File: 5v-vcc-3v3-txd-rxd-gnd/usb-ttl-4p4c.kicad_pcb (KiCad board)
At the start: 4 copper layers, 41.3 x 16.5 mm, 3 parts, among them J1 4P4C, P1 CONN_6X1

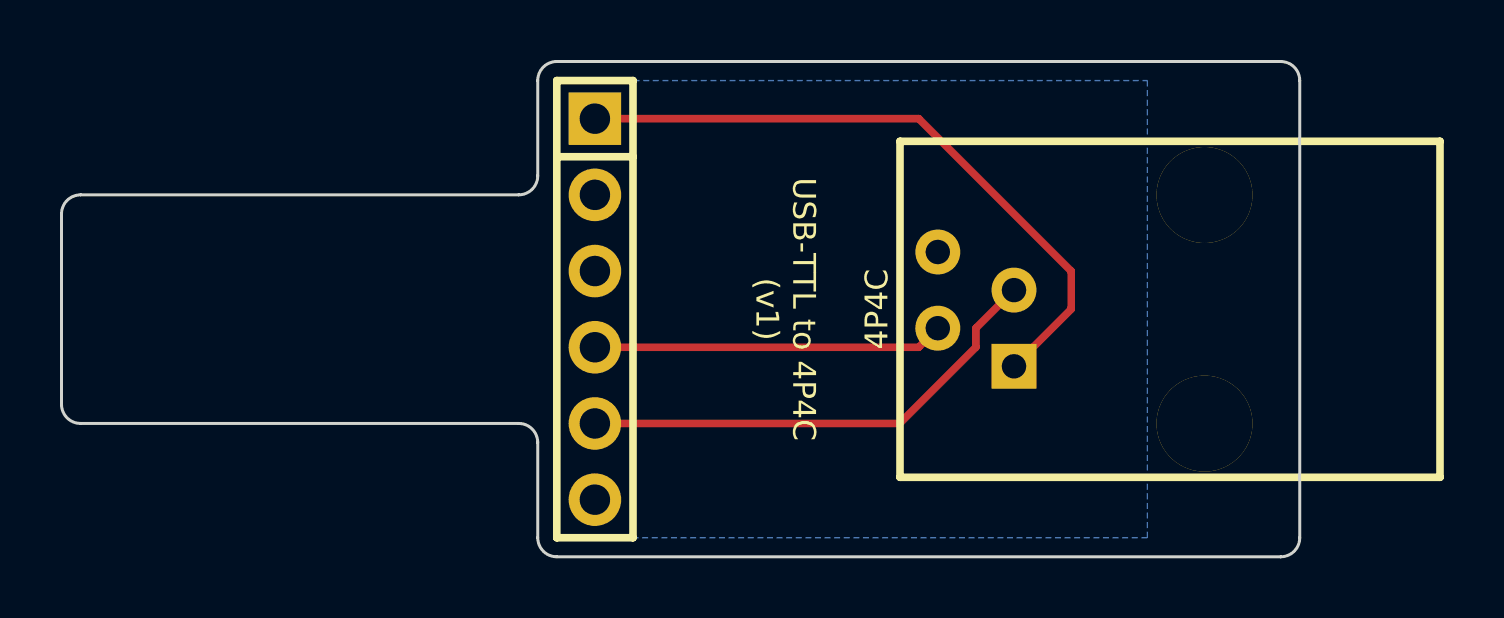
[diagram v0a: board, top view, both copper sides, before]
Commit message: adding a diode
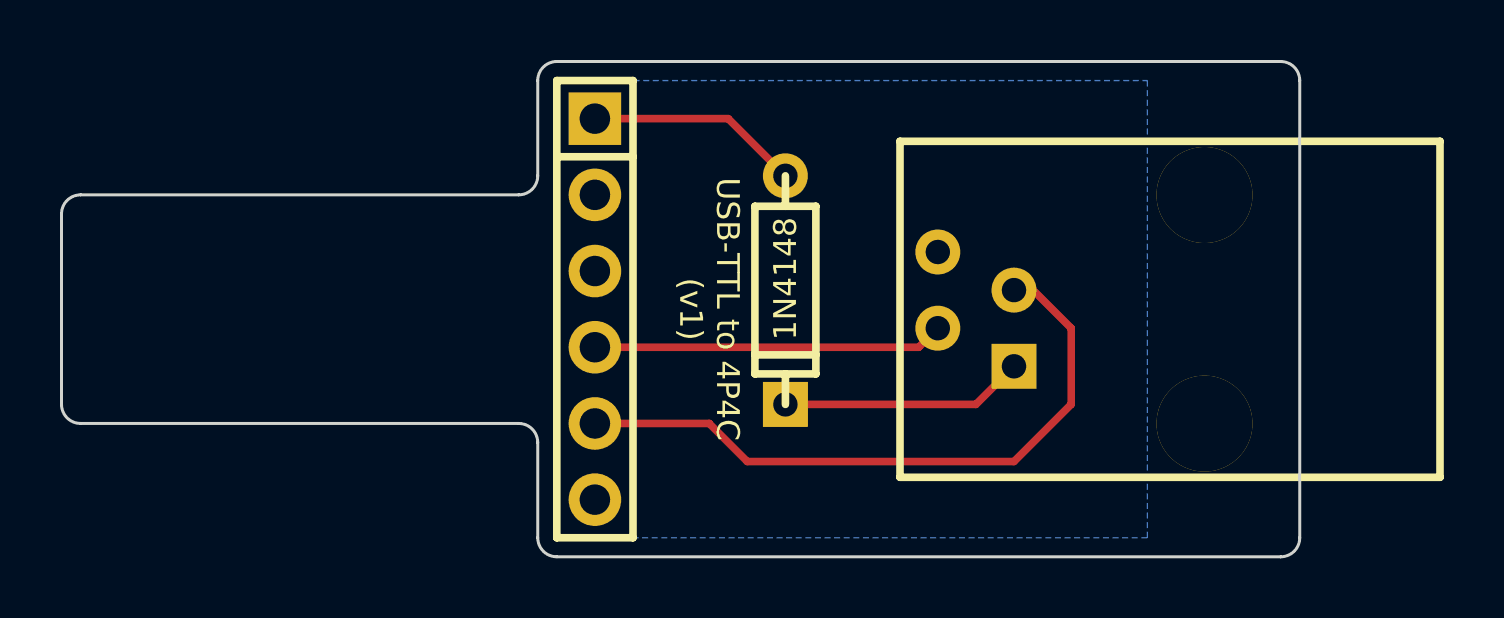
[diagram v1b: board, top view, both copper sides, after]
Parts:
- added D1: 1N4148, DIODE_SS_059A_03_PL, F.Cu at (180.3, 110.5)
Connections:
- J1 pad 1: 5V -> N-000007
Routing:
- net 5V: track 21.9 -> 7.14 mm
- net N-000007: track 0.00 -> 8.15 mm
- net RXD: track 16.2 -> 22.2 mm
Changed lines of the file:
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@@
 (kicad_pcb (version 3) (host pcbnew "(22-Jun-2014 BZR 4027)-stable")
   (general
-    (links 4)
+    (links 5)
     (no_connects 0)
-    (area 156.159999 104.089999 197.535001 118.160001)
+    (area 156.159999 102.819999 197.535001 119.430001)
     (thickness 1.6)
     (drawings 28)
-    (tracks 10)
+    (tracks 13)
     (zones 0)
-    (modules 3)
-    (nets 5)
+    (modules 4)
+    (nets 6)
   )
   (page A3)
@@
   (net 1 5V)
   (net 2 GND)
-  (net 3 RXD)
-  (net 4 TXD)
+  (net 3 N-000007)
+  (net 4 RXD)
+  (net 5 TXD)
   (net_class Default "This is the default net class."
     (clearance 0.254)
@@
     (add_net 5V)
     (add_net GND)
+    (add_net N-000007)
     (add_net RXD)
     (add_net TXD)
@@
       (effects (font (size 1.016 1.016) (thickness 0.2032)))
     )
-    (fp_text value 4P4C (at 1.905 -4.572 90) (layer F.SilkS)
+    (fp_text value 4P4C (at 1.905 -4.572 90) (layer F.SilkS) hide
       (effects (font (size 0.762 0.762) (thickness 0.1524)))
     )
@@
     (pad 2 thru_hole circle (at 1.27 -2.54 90) (size 1.4986 1.4986) (drill 0.8128)
       (layers *.Cu *.Mask F.SilkS)
-      (net 4 TXD)
+      (net 5 TXD)
     )
     (pad 4 thru_hole circle (at 3.81 -2.54 90) (size 1.4986 1.4986) (drill 0.8128)
@@
     (pad 1 thru_hole rect (at 0 0 90) (size 1.4986 1.4986) (drill 0.8128)
       (layers *.Cu *.Mask F.SilkS)
-      (net 1 5V)
+      (net 3 N-000007)
     )
     (pad 3 thru_hole circle (at 2.54 0 90) (size 1.4986 1.4986) (drill 0.8128)
       (layers *.Cu *.Mask F.SilkS)
-      (net 3 RXD)
+      (net 4 RXD)
     )
     (pad "" thru_hole circle (at 5.71 6.35 90) (size 3.2 3.2) (drill 3.2)
@@
     (pad 4 thru_hole circle (at 5.08 0 270) (size 1.7526 1.7526) (drill 1.016)
       (layers *.Cu *.Mask F.SilkS)
-      (net 4 TXD)
+      (net 5 TXD)
     )
     (pad 5 thru_hole circle (at 7.62 0 270) (size 1.7526 1.7526) (drill 1.016)
       (layers *.Cu *.Mask F.SilkS)
-      (net 3 RXD)
+      (net 4 RXD)
     )
     (pad 6 thru_hole circle (at 10.16 0 270) (size 1.7526 1.7526) (drill 1.016)
       (layers *.Cu *.Mask F.SilkS)
       (net 2 GND)
+    )
+  )
+  (module DIODE_SS_059A_03_PL (layer F.Cu)
+    (at 180.34 110.49 270)
+    (descr "Small-signal diode, 0.3\"")
+    (tags "DIODE DEV")
+    (fp_text reference D1 (at 0 -1.651 270) (layer F.SilkS) hide
+      (effects (font (size 0.762 0.762) (thickness 0.1524)))
+    )
+    (fp_text value 1N4148 (at -0.381 0 270) (layer F.SilkS)
+      (effects (font (size 0.762 0.762) (thickness 0.1524)))
+    )
+    (fp_line (start -2.794 0) (end -3.81 0) (layer F.SilkS) (width 0.254))
+    (fp_line (start 2.794 0) (end 3.81 0) (layer F.SilkS) (width 0.254))
+    (fp_line (start -2.794 1.016) (end 2.794 1.016) (layer F.SilkS) (width 0.254))
+    (fp_line (start 2.794 -1.016) (end -2.794 -1.016) (layer F.SilkS) (width 0.254))
+    (fp_line (start 2.159 -1.016) (end 2.159 1.016) (layer F.SilkS) (width 0.254))
+    (fp_line (start 2.794 0) (end 2.794 -1.016) (layer F.SilkS) (width 0.254))
+    (fp_line (start -2.794 -1.016) (end -2.794 0) (layer F.SilkS) (width 0.254))
+    (fp_line (start -2.794 0) (end -2.794 1.016) (layer F.SilkS) (width 0.254))
+    (fp_line (start 2.794 1.016) (end 2.794 0) (layer F.SilkS) (width 0.254))
+    (pad 2 thru_hole rect (at 3.81 0 270) (size 1.4986 1.4986) (drill 0.8128)
+      (layers *.Cu *.Mask F.SilkS)
+      (net 3 N-000007)
+    )
+    (pad 1 thru_hole oval (at -3.81 0 270) (size 1.4986 1.4986) (drill 0.8128)
+      (layers *.Cu *.Mask F.SilkS)
+      (net 1 5V)
+    )
+    (model discret/diode.wrl
+      (at (xyz 0 0 0))
+      (scale (xyz 0.3 0.3 0.3))
+      (rotate (xyz 0 0 0))
     )
   )
@@
     (effects (font (size 0.762 0.762) (thickness 0.1524)) (justify right mirror))
   )
-  (gr_text "USB-TTL to 4P4C\n(v1)" (at 180.34 111.125 270) (layer F.SilkS)
+  (gr_text "USB-TTL to 4P4C\n(v1)" (at 177.8 111.125 270) (layer F.SilkS)
     (effects (font (size 0.762 0.762) (thickness 0.1524)))
   )
@@
     (effects (font (size 0.762 0.762) (thickness 0.1524)) (justify right mirror))
   )
-  (segment (start 173.99 104.775) (end 184.785 104.775) (width 0.254) (layer F.Cu) (net 1) (status 400000))
-  (segment (start 189.865 111.125) (end 187.96 113.03) (width 0.254) (layer F.Cu) (net 1) (status 800000))
-  (segment (start 189.865 109.855) (end 189.865 111.125) (width 0.254) (layer F.Cu) (net 1))
-  (segment (start 184.785 104.775) (end 189.865 109.855) (width 0.254) (layer F.Cu) (net 1))
-  (segment (start 173.99 114.935) (end 184.15 114.935) (width 0.254) (layer F.Cu) (net 3) (status 400000))
-  (segment (start 186.69 111.76) (end 187.96 110.49) (width 0.254) (layer F.Cu) (net 3) (status 800000))
-  (segment (start 186.69 112.395) (end 186.69 111.76) (width 0.254) (layer F.Cu) (net 3))
-  (segment (start 184.15 114.935) (end 186.69 112.395) (width 0.254) (layer F.Cu) (net 3))
-  (segment (start 173.99 112.395) (end 184.785 112.395) (width 0.254) (layer F.Cu) (net 4) (status 400000))
-  (segment (start 184.785 112.395) (end 185.42 111.76) (width 0.254) (layer F.Cu) (net 4) (status 800000))
+  (segment (start 173.99 104.775) (end 178.435 104.775) (width 0.254) (layer F.Cu) (net 1) (status 400000))
+  (segment (start 178.435 104.775) (end 180.34 106.68) (width 0.254) (layer F.Cu) (net 1) (status 800000))
+  (segment (start 180.34 114.3) (end 186.69 114.3) (width 0.254) (layer F.Cu) (net 3) (status 400000))
+  (segment (start 186.69 114.3) (end 187.96 113.03) (width 0.254) (layer F.Cu) (net 3) (status 800000))
+  (segment (start 173.99 114.935) (end 177.8 114.935) (width 0.254) (layer F.Cu) (net 4) (status 400000))
+  (segment (start 188.595 110.49) (end 187.96 110.49) (width 0.254) (layer F.Cu) (net 4) (status C00000))
+  (segment (start 189.865 111.76) (end 188.595 110.49) (width 0.254) (layer F.Cu) (net 4) (status 800000))
+  (segment (start 189.865 114.3) (end 189.865 111.76) (width 0.254) (layer F.Cu) (net 4))
+  (segment (start 187.96 116.205) (end 189.865 114.3) (width 0.254) (layer F.Cu) (net 4))
+  (segment (start 179.07 116.205) (end 187.96 116.205) (width 0.254) (layer F.Cu) (net 4))
+  (segment (start 177.8 114.935) (end 179.07 116.205) (width 0.254) (layer F.Cu) (net 4))
+  (segment (start 173.99 112.395) (end 184.785 112.395) (width 0.254) (layer F.Cu) (net 5) (status 400000))
+  (segment (start 184.785 112.395) (end 185.42 111.76) (width 0.254) (layer F.Cu) (net 5) (status 800000))
   (zone (net 2) (net_name GND) (layer B.Cu) (hatch edge 0.508)
     (connect_pads (clearance 0.508))
